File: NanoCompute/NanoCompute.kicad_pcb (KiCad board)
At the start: 2 copper layers, 62 parts, among them J1 2250506, U1 RTL8211F, U2 MT53E1G32D2FW, U3 HSP051, U4 RK3588, U5 TPS54308, U6 HSP051, U7 TLV74311, U8 TLV74325, Y1 25 MHz

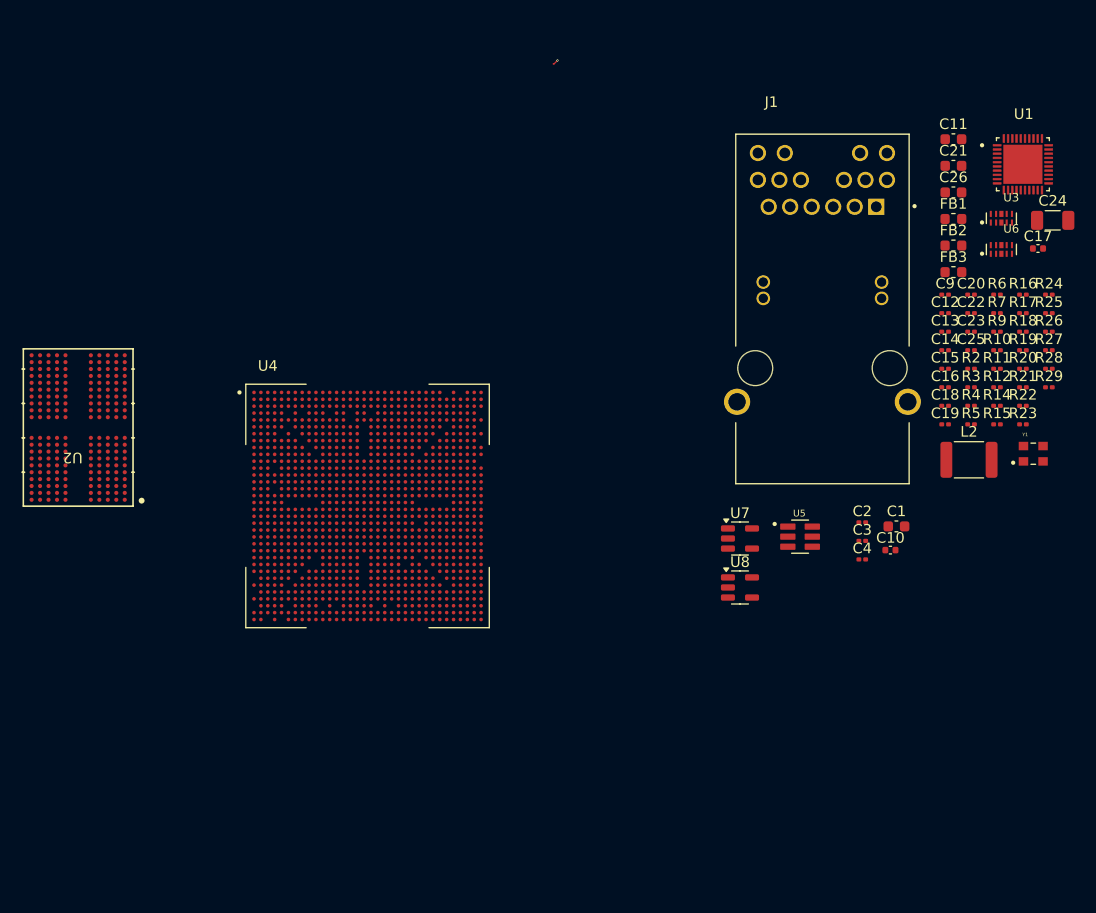
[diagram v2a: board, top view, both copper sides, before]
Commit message: LPDDR4 second chip connected to LPDDR4 PHY
Added a missing Units for second LPDDR4 chip (VSS and Power).
Added a 1x100nF decoupling capacitor for each power rail of VDD1 but it
seems too much. Might need to find a better way of doing Low-Mid-High
range frequency decoupling.
Added TPS65296 as a LPddr4 Memory power solution but I need to check if
I can power both memory chips with just one TPS65296.
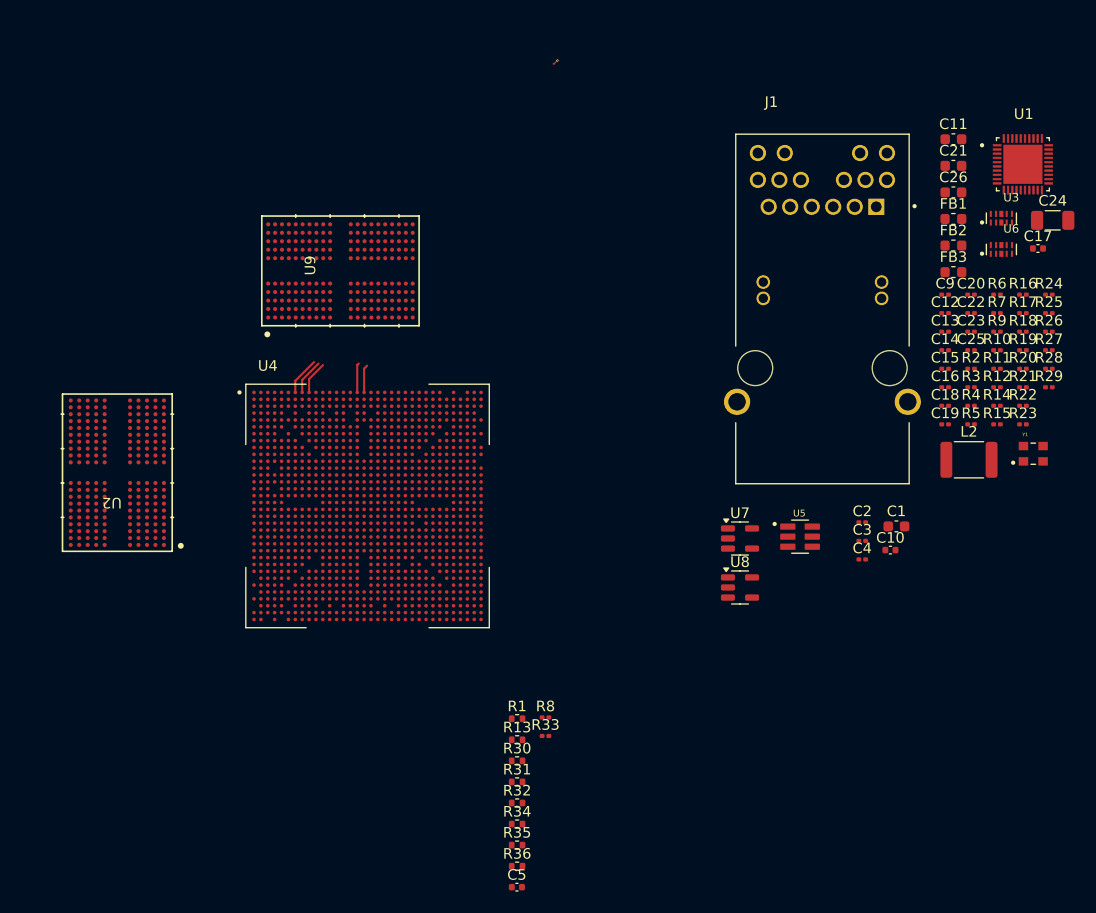
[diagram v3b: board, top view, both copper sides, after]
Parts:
- added C5: 100n, Capacitor_SMD:C_0402_1005Metric, F.Cu at (133.3, 125.5)
- added R1: 240R, Resistor_SMD:R_0402_1005Metric, F.Cu at (133.3, 109.6)
- added R13: 240R, Resistor_SMD:R_0402_1005Metric, F.Cu at (133.3, 111.6)
- added R30: 240R, Resistor_SMD:R_0402_1005Metric, F.Cu at (133.3, 113.6)
- added R31: 240R, Resistor_SMD:R_0402_1005Metric, F.Cu at (133.3, 115.5)
- added R32: 240R, Resistor_SMD:R_0402_1005Metric, F.Cu at (133.3, 117.5)
- added R33: 10K, Resistor_SMD:R_0201_0603Metric, F.Cu at (136.0, 111.2)
- added R34: 240R, Resistor_SMD:R_0402_1005Metric, F.Cu at (133.3, 119.5)
- added R35: 240R, Resistor_SMD:R_0402_1005Metric, F.Cu at (133.3, 121.5)
- added R36: 240R, Resistor_SMD:R_0402_1005Metric, F.Cu at (133.3, 123.5)
- added R8: 10K, Resistor_SMD:R_0201_0603Metric, F.Cu at (136.0, 109.5)
- added U9: MT53E1G32D2FW, CBFtLib:VFBGA200_10X14.5X1.1FW_MRN, F.Cu at (116.7, 67.3)
- moved U2 5.65 mm to (95.6, 86.3)
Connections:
- U2 pad A5: unconnected-(U2A-ZQ0-PadA5) -> Net-(U2A-ZQ0)
- U2 pad A8: unconnected-(U2A-ZQ1-PadA8) -> Net-(U2A-ZQ1)
- U2 pad D10: unconnected-(U2A-DQS1_t_A-PadD10) -> /LPDDR4/DQS1_A_P
- U2 pad D3: unconnected-(U2A-DQS0_t_A-PadD3) -> /LPDDR4/DQS0_A_P
- U2 pad E10: unconnected-(U2A-DQS1_c_A-PadE10) -> /LPDDR4/DQS1_A_N
- U2 pad E3: unconnected-(U2A-DQS0_c_A-PadE3) -> /LPDDR4/DQS0_A_N
- U2 pad G2: unconnected-(U2A-ODT_CA_A-PadG2) -> VDD2_DDR
- U2 pad P11: /LPDDR4/CA5_A -> /LPDDR4/CA5_B
- U2 pad P2: /LPDDR4/CA1_A -> /LPDDR4/CA1_B
- U2 pad P4: /LPDDR4/CKE0_A -> /LPDDR4/CKE0_B
- U2 pad P5: /LPDDR4/CKE1_A -> /LPDDR4/CKE1_B
- U2 pad R10: /LPDDR4/CA3_A -> /LPDDR4/CA3_B
- U2 pad R11: /LPDDR4/CA4_A -> /LPDDR4/CA4_B
- U2 pad R2: /LPDDR4/CA0_A -> /LPDDR4/CA0_B
- U2 pad R3: /LPDDR4/CS0_A -> /LPDDR4/CS1_B
- U2 pad R4: /LPDDR4/CS1_A -> /LPDDR4/CS0_B
- U2 pad R9: /LPDDR4/CA2_A -> /LPDDR4/CA2_B
- U2 pad T11: unconnected-(U2A-RESET_n-PadT11) -> /LPDDR4/~{RESET}_AB
- U2 pad T2: unconnected-(U2A-ODT_CA_B-PadT2) -> VDD2_DDR
- U2 pad V10: unconnected-(U2A-DQS1_c_B-PadV10) -> /LPDDR4/DQS1_B_N
- U2 pad V3: unconnected-(U2A-DQS0_c_B-PadV3) -> /LPDDR4/DQS0_B_N
- U2 pad W10: unconnected-(U2A-DQS1_t_B-PadW10) -> /LPDDR4/DQS1_B_P
- U2 pad W3: unconnected-(U2A-DQS0_t_B-PadW3) -> /LPDDR4/DQS0_B_P
- U2 pad Y10: /LPDDR4/DMI1_A -> /LPDDR4/DMI1_B
- U2 pad Y3: /LPDDR4/DMIO_A -> /LPDDR4/DMIO_B
- U4 pad A10: (no net) -> /LPDDR4/CA4_C
- U4 pad A12: (no net) -> /LPDDR4/CK_C_N
- U4 pad A13: (no net) -> /LPDDR4/CK_D_N
- U4 pad A15: (no net) -> /LPDDR4/CA4_D
- U4 pad A16: (no net) -> /LPDDR4/DQ2_D
- U4 pad A17: (no net) -> /LPDDR4/DQ0_D
- U4 pad A18: (no net) -> /LPDDR4/DQ6_D
- U4 pad A19: (no net) -> /LPDDR4/DQ4_D
- U4 pad A2: (no net) -> /LPDDR4/DQ10_C
- U4 pad A20: (no net) -> /LPDDR4/DQ12_D
- U4 pad A21: (no net) -> /LPDDR4/DQ14_D
- U4 pad A22: (no net) -> /LPDDR4/DQ8_D
- U4 pad A23: (no net) -> /LPDDR4/DQ10_D
- U4 pad A3: (no net) -> /LPDDR4/DQ8_C
- U4 pad A4: (no net) -> /LPDDR4/DQ14_C
- U4 pad A5: (no net) -> /LPDDR4/DQ12_C
- U4 pad A6: (no net) -> /LPDDR4/DQ4_C
- U4 pad A7: (no net) -> /LPDDR4/DQ6_C
- U4 pad A8: (no net) -> /LPDDR4/DQ0_C
- U4 pad A9: (no net) -> /LPDDR4/DQ2_C
- U4 pad AA4: unconnected-(U4A-DDR_CH0_DQS1N_A-PadAA4) -> /LPDDR4/DQS1_A_N
- U4 pad AA5: unconnected-(U4A-DDR_CH0_DQS1P_A-PadAA5) -> /LPDDR4/DQS1_A_P
- U4 pad AB4: unconnected-(U4A-DDR_CH0_DM1_A-PadAB4) -> /LPDDR4/DMI1_A
- U4 pad B10: (no net) -> /LPDDR4/DQ3_C
- U4 pad B11: (no net) -> /LPDDR4/CA5_C
- U4 pad B12: (no net) -> /LPDDR4/CK_C_P
- U4 pad B13: (no net) -> /LPDDR4/CK_D_P
- U4 pad B14: (no net) -> /LPDDR4/CA5_D
- U4 pad B15: (no net) -> /LPDDR4/DQ3_D
- U4 pad B16: (no net) -> /LPDDR4/DQ1_D
- U4 pad B17: (no net) -> /LPDDR4/DQ7_D
- U4 pad B18: (no net) -> /LPDDR4/DQ5_D
- U4 pad B2: (no net) -> /LPDDR4/DQ11_C
- U4 pad B20: (no net) -> /LPDDR4/DQ13_D
- U4 pad B21: (no net) -> /LPDDR4/DQ15_D
- U4 pad B22: (no net) -> /LPDDR4/DQ9_D
- U4 pad B23: (no net) -> /LPDDR4/DQ11_D
- U4 pad B3: (no net) -> /LPDDR4/DQ9_C
- U4 pad B4: (no net) -> /LPDDR4/DQ15_C
- U4 pad B5: (no net) -> /LPDDR4/DQ13_C
- U4 pad B7: (no net) -> /LPDDR4/DQ5_C
- U4 pad B8: (no net) -> /LPDDR4/DQ7_C
- U4 pad B9: (no net) -> /LPDDR4/DQ1_C
- U4 pad C19: (no net) -> unconnected-(U4B-DDR_CH1_RESET_D-PadC19)
- U4 pad D10: (no net) -> unconnected-(U4B-DDR_CH1_A6_C-PadD10)
- U4 pad D11: (no net) -> /LPDDR4/CKE0_C
- U4 pad D13: (no net) -> /LPDDR4/CA3_C
- U4 pad D14: (no net) -> unconnected-(U4B-DDR_CH1_A6_D-PadD14)
- U4 pad D16: (no net) -> /LPDDR4/CKE0_D
- U4 pad D17: (no net) -> unconnected-(U4B-DDR_CH1_WCK0N_D-PadD17)
- U4 pad D19: (no net) -> /LPDDR4/CS1_D
- U4 pad D20: (no net) -> /LPDDR4/DMIO_D
- U4 pad D21: (no net) -> /LPDDR4/DQS1_D_P
- U4 pad D22: (no net) -> /LPDDR4/DMI1_D
- U4 pad D4: (no net) -> /LPDDR4/DMI1_C
- U4 pad D5: (no net) -> /LPDDR4/DQS1_C_N
- U4 pad D7: (no net) -> unconnected-(U4B-DDR_CH1_WCK1P_C-PadD7)
- U4 pad D9: (no net) -> /LPDDR4/DQS0_C_N
- U4 pad E10: (no net) -> /LPDDR4/~{RESET}_CD
- U4 pad E11: (no net) -> /LPDDR4/CKE1_C
- U4 pad E13: (no net) -> /LPDDR4/CA2_C
- U4 pad E14: (no net) -> /LPDDR4/CA3_D
- U4 pad E16: (no net) -> /LPDDR4/CKE1_D
- U4 pad E17: (no net) -> unconnected-(U4B-DDR_CH1_WCK0P_D-PadE17)
- U4 pad E19: (no net) -> /LPDDR4/CS0_D
- U4 pad E21: (no net) -> /LPDDR4/DQS1_D_N
- U4 pad E4: unconnected-(U4A-DDR_CH0_DM1_B-PadE4) -> /LPDDR4/DMI1_B
- U4 pad E5: (no net) -> /LPDDR4/DQS1_C_P
- U4 pad E7: (no net) -> unconnected-(U4B-DDR_CH1_WCK1N_C-PadE7)
- U4 pad E9: (no net) -> /LPDDR4/DQS0_C_P
- U4 pad F12: (no net) -> /LPDDR4/CA1_C
- U4 pad F18: (no net) -> Net-(U4B-DDR_CH1_ZQ_D)
- U4 pad F4: unconnected-(U4A-DDR_CH0_DQS1N_B-PadF4) -> /LPDDR4/DQS1_B_N
- U4 pad F5: unconnected-(U4A-DDR_CH0_DQS1P_B-PadF5) -> /LPDDR4/DQS1_B_P
- U4 pad F8: (no net) -> /LPDDR4/DMIO_C
- U4 pad G11: (no net) -> /LPDDR4/CS0_C
- U4 pad G12: (no net) -> /LPDDR4/CA0_C
- U4 pad G13: (no net) -> /LPDDR4/CA2_D
- U4 pad G14: (no net) -> /LPDDR4/CA1_D
- U4 pad G16: (no net) -> /LPDDR4/DQS0_D_N
- U4 pad G18: (no net) -> unconnected-(U4B-DDR_CH1_WCK1N_D-PadG18)
- U4 pad G4: unconnected-(U4A-DDR_CH0_DM0_B-PadG4) -> /LPDDR4/DMIO_B
- U4 pad G8: (no net) -> Net-(U4B-DDR_CH1_ZQ_C)
- U4 pad G9: (no net) -> unconnected-(U4B-DDR_CH1_WCK0P_C-PadG9)
- U4 pad H11: (no net) -> /LPDDR4/CS1_C
- U4 pad H13: (no net) -> unconnected-(U4B-DDR_CH1_VDDQ_CKE-PadH13)
- U4 pad H15: (no net) -> /LPDDR4/CA0_D
- U4 pad H16: (no net) -> /LPDDR4/DQS0_D_P
- U4 pad H18: (no net) -> unconnected-(U4B-DDR_CH1_WCK1P_D-PadH18)
- U4 pad H7: unconnected-(U4A-DDR_CH0_ZQ_B-PadH7) -> Net-(U4A-DDR_CH0_ZQ_B)
- U4 pad H9: (no net) -> unconnected-(U4B-DDR_CH1_WCK0N_C-PadH9)
- U4 pad J7: unconnected-(U4A-DDR_CH0_DQS0N_B-PadJ7) -> /LPDDR4/DQS0_B_N
- U4 pad J8: unconnected-(U4A-DDR_CH0_DQS0P_B-PadJ8) -> /LPDDR4/DQS0_B_P
- U4 pad K1: unconnected-(U4A-DDR_CH0_A4_B-PadK1) -> /LPDDR4/CA4_B
- U4 pad K11: (no net) -> unconnected-(U4B-DDR_CH1_VDDQ_0-PadK11)
- U4 pad K12: (no net) -> unconnected-(U4B-DDR_CH1_VDDQ_1-PadK12)
- U4 pad K13: (no net) -> unconnected-(U4B-DDR_CH1_VDDQ_2-PadK13)
- U4 pad K14: (no net) -> unconnected-(U4B-DDR_CH1_VDDQ_3-PadK14)
- U4 pad K15: (no net) -> unconnected-(U4B-DDR_CH1_VDDQ_4-PadK15)
- U4 pad K16: (no net) -> unconnected-(U4B-DDR_CH1_PLL_AVDD1V8-PadK16)
- U4 pad L11: (no net) -> unconnected-(U4B-DDR_CH1_VDD_0-PadL11)
- U4 pad L12: (no net) -> unconnected-(U4B-DDR_CH1_VDD_1-PadL12)
- U4 pad L13: (no net) -> unconnected-(U4B-DDR_CH1_VDD_2-PadL13)
- U4 pad L14: (no net) -> unconnected-(U4B-DDR_CH1_VDD_3-PadL14)
- U4 pad L15: (no net) -> unconnected-(U4B-DDR_CH1_PLL_DVDD-PadL15)
- U4 pad L16: (no net) -> GND
- U4 pad L17: (no net) -> unconnected-(U4B-DDR_CH1_VDD_MIF_0-PadL17)
- U4 pad L18: (no net) -> unconnected-(U4B-DDR_CH1_VDD_MIF_1-PadL18)
- U4 pad L2: unconnected-(U4A-DDR_CH0_A5_B-PadL2) -> /LPDDR4/CA5_B
- U4 pad L4: unconnected-(U4A-DDR_CH0_LP4/4X_CKE1/LP5_CS1_B-PadL4) -> /LPDDR4/CKE1_B
- U4 pad L5: unconnected-(U4A-DDR_CH0_LP4/4X_CKE0/LP5_CS0_B-PadL5) -> /LPDDR4/CKE0_B
- U4 pad L7: unconnected-(U4A-DDR_CH0_LP4/4X_CS0_B-PadL7) -> /LPDDR4/CS0_B
- U4 pad L8: unconnected-(U4A-DDR_CH0_LP4/4X_CS1_B-PadL8) -> /LPDDR4/CS1_B
- U4 pad M1: unconnected-(U4A-DDR_CH0_CKB_B-PadM1) -> /LPDDR4/CK_A_N
- U4 pad M11: unconnected-(U4A-DDR_CH0_PLL_AVSS-PadM11) -> GND
- U4 pad M13: (no net) -> unconnected-(U4B-DDR_CH1_VDDQ_CK-PadM13)
- U4 pad M2: unconnected-(U4A-DDR_CH0_CK_B-PadM2) -> /LPDDR4/CK_A_P
- U4 pad M5: unconnected-(U4A-DDR_CH0_A1_B-PadM5) -> /LPDDR4/CA1_B
- U4 pad M8: unconnected-(U4A-DDR_CH0_A0_B-PadM8) -> /LPDDR4/CA0_B
- U4 pad N1: unconnected-(U4A-DDR_CH0_CKB_A-PadN1) -> /LPDDR4/CK_A_N
- U4 pad N2: unconnected-(U4A-DDR_CH0_CK_A-PadN2) -> /LPDDR4/CK_A_P
- U4 pad N4: unconnected-(U4A-DDR_CH0_A3_B-PadN4) -> /LPDDR4/CA3_B
- U4 pad N5: unconnected-(U4A-DDR_CH0_A2_B-PadN5) -> /LPDDR4/CA2_B
- U4 pad T4: unconnected-(U4A-DDR_CH0_RESET_A-PadT4) -> /LPDDR4/~{RESET}_AB
- U4 pad U4: unconnected-(U4A-DDR_CH0_DQS0N_A-PadU4) -> /LPDDR4/DQS0_A_N
- U4 pad U5: unconnected-(U4A-DDR_CH0_DQS0P_A-PadU5) -> /LPDDR4/DQS0_A_P
- U4 pad W8: unconnected-(U4A-DDR_CH0_ZQ_A-PadW8) -> Net-(U4A-DDR_CH0_ZQ_A)
- U4 pad Y4: unconnected-(U4A-DDR_CH0_DM0_A-PadY4) -> /LPDDR4/DMIO_A
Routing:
- net /LPDDR4/DQ6_C: track 0.00 -> 3.60 mm
- net /LPDDR4/DQ0_C: track 0.00 -> 3.36 mm
- net /LPDDR4/DQ2_C: track 0.00 -> 3.12 mm
- net /LPDDR4/DQ2_D: track 0.00 -> 2.79 mm
- net /LPDDR4/DQ0_D: track 0.00 -> 2.64 mm
